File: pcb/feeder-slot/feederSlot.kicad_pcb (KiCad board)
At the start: 2 copper layers, 13.4 x 31.1 mm, 6 parts, among them J2 Conn_01x05_Female, J3 Conn_01x04_Pin, U1 DS28E07

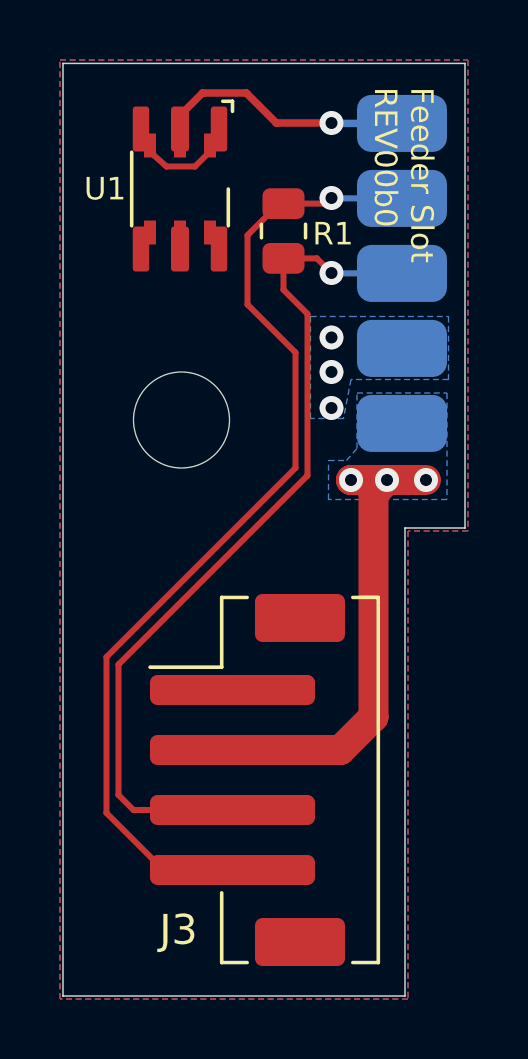
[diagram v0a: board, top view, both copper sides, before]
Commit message: updates placement for silk on feeder-slot
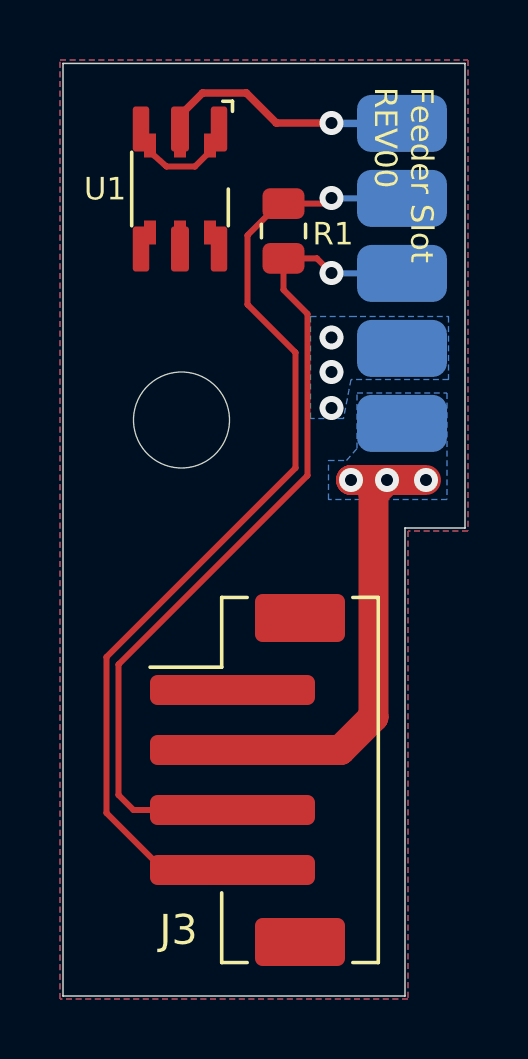
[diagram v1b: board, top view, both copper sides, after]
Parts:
- moved G*** 19.5 mm to (26.9, 48.8)
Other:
- board text added: "Feeder Slot REV00"
- board text removed: "Feeder Slot REV00b0"
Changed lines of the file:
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@@
 	(footprint "index:logo"
 		(layer "B.Cu")
-		(at 26 29.3 180)
+		(at 26.95 48.8 180)
 		(property "Reference" "G***"
 			(at 0 0 0)
@@
 		(layer "Edge.Cuts")
 	)
-	(gr_text "Feeder Slot\nREV00b0"
+	(gr_text "Feeder Slot\nREV00"
 		(at 32.6 25.9 270)
 		(layer "F.SilkS")
